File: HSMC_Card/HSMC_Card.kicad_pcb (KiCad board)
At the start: 2 copper layers, 25.4 x 78.1 mm, 5 parts, among them J1 HSMC_Card_ASP

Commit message: Minor adjustments to HSMC_Card PCB
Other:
- board text added: "Host Board Edge 5mm Verical Clearance"
- board text removed: "Host Board Edge 0.5mm Verical Clearance"
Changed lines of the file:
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@@
   (general
     (thickness 1.6)
-    (drawings 5)
+    (drawings 6)
     (tracks 0)
     (zones 0)
@@
     (pad_to_mask_clearance 0.051)
     (solder_mask_min_width 0.25)
-    (aux_axis_origin 0 0)
+    (aux_axis_origin 25.4 25.4)
     (visible_elements FFFFFF7F)
     (pcbplotparams
@@
     (pad "" np_thru_hole circle (at 0 0) (size 3.175 3.175) (drill 3.175) (layers *.Cu *.Mask))
   )
-  (gr_text "Host Board Edge\n0.5mm Verical Clearance" (at 46.99 64.4652 270) (layer Cmts.User)
+  (dimension 78.105 (width 0.3) (layer Cmts.User)
+    (gr_text "3.0760 in" (at 21.395 64.4525 90) (layer Cmts.User)
+      (effects (font (size 1.5 1.5) (thickness 0.3)))
+    )
+    (feature1 (pts (xy 24.765 25.4) (xy 22.908579 25.4)))
+    (feature2 (pts (xy 24.765 103.5304) (xy 22.908579 103.5304)))
+    (crossbar (pts (xy 23.495 103.5304) (xy 23.495 25.4)))
+    (arrow1a (pts (xy 23.495 25.4) (xy 24.081421 26.526504)))
+    (arrow1b (pts (xy 23.495 25.4) (xy 22.908579 26.526504)))
+    (arrow2a (pts (xy 23.495 103.5304) (xy 24.081421 102.378496)))
+    (arrow2b (pts (xy 23.495 103.5304) (xy 22.908579 102.378496)))
+  )
+  (gr_text "Host Board Edge\n5mm Verical Clearance" (at 46.99 64.4652 270) (layer Cmts.User)
     (effects (font (size 1 1) (thickness 0.12)))
   )

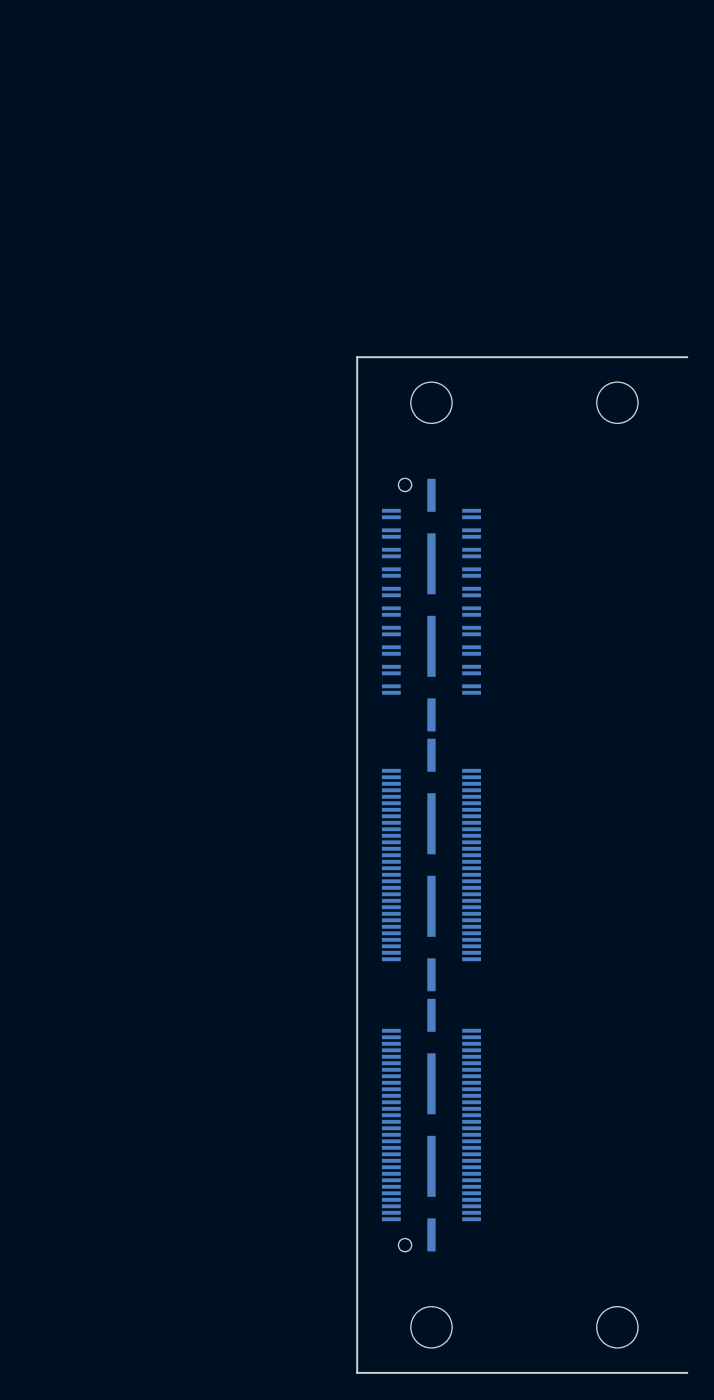
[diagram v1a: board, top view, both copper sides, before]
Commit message: Update version of HSMC_Card_ASP symbol, minor adjustments to PCB layout template.
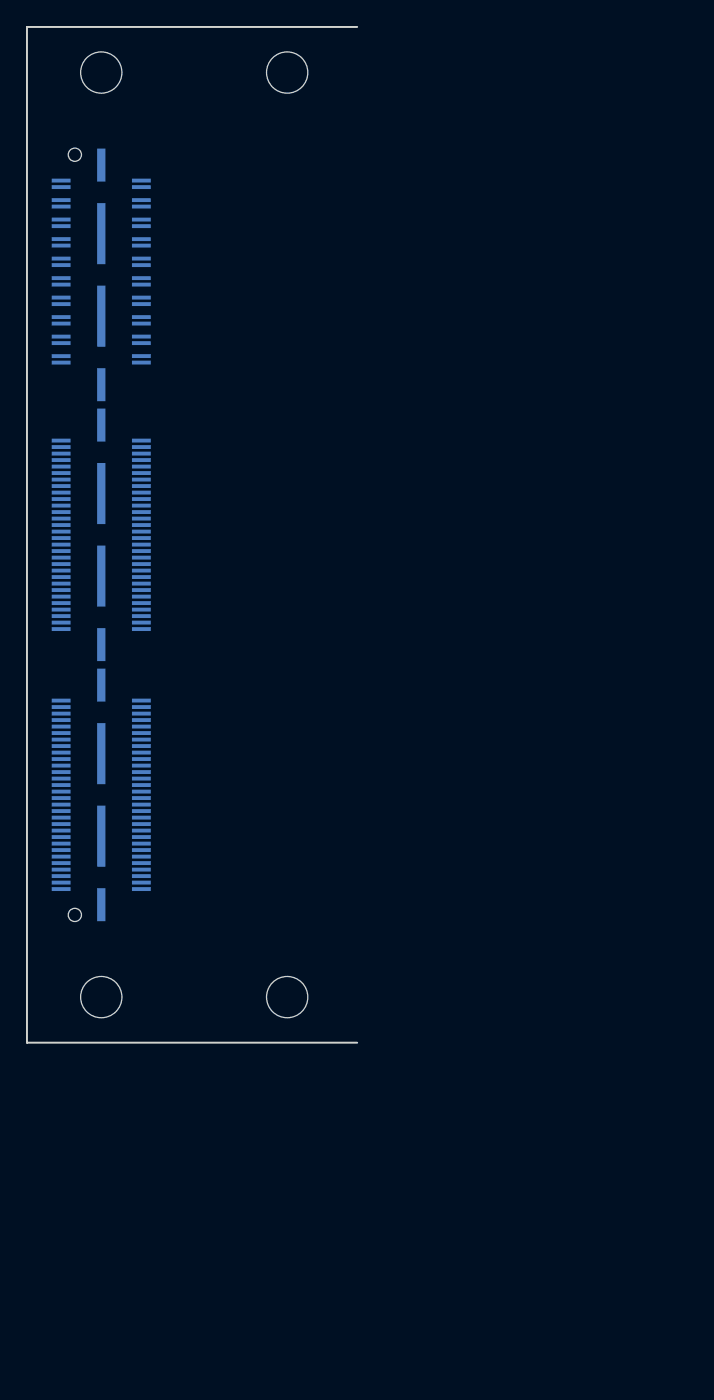
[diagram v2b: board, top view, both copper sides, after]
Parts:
- moved J1 35.9 mm to (5.71, 39.1)
- moved MH1 35.9 mm to (5.71, 3.51)
- moved MH3 35.9 mm to (20.0, 3.51)
- moved MH2 35.9 mm to (5.71, 74.6)
- moved MH4 35.9 mm to (20.0, 74.6)
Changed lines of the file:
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@@
-(kicad_pcb (version 20171130) (host pcbnew 5.0.1)
+(kicad_pcb (version 20171130) (host pcbnew 5.1.1)
   (general
     (thickness 1.6)
@@
     (zone_45_only no)
     (trace_min 0.2)
-    (segment_width 0.2)
-    (edge_width 0.15)
     (via_size 0.8)
     (via_drill 0.4)
@@
     (uvia_min_size 0.2)
     (uvia_min_drill 0.1)
+    (edge_width 0.15)
+    (segment_width 0.2)
     (pcb_text_width 0.3)
     (pcb_text_size 1.5 1.5)
@@
     (pad_to_mask_clearance 0.051)
     (solder_mask_min_width 0.25)
-    (aux_axis_origin 25.4 25.4)
-    (visible_elements FFFFFF7F)
+    (aux_axis_origin 0 0)
+    (visible_elements FEFFFF7F)
     (pcbplotparams
       (layerselection 0x010fc_ffffffff)
@@
     (add_net "Net-(J1-Pad98)")
   )
-  (module Connector_Samtec:Samtec_HSMC_ASP-122952-01_P0.5mm_Vertical locked (layer B.Cu)
-    (at 31.115 64.4652 270)
+  (module Connector_Samtec:Samtec_HSMC_ASP-122952-01_P0.5mm_Vertical (layer B.Cu)
+    (at 5.715 39.0652 270)
     (descr http://suddendocs.samtec.com/prints/asp-122952-01-mkt.pdf)
     (tags "Samtec HSMC card mezzanine vertical")
@@
   )
   (module MountingHole:MoutingHole_0.125in locked (layer F.Cu)
-    (at 45.4152 28.9052)
+    (at 20.0152 3.5052)
     (attr virtual)
     (fp_text reference MH3 (at 0 -4.5) (layer F.SilkS) hide
@@
   )
   (module MountingHole:MoutingHole_0.125in locked (layer F.Cu)
-    (at 45.4152 100.0252)
+    (at 20.0152 74.6252)
     (attr virtual)
     (fp_text reference MH4 (at 0 -4.5) (layer F.SilkS) hide
@@
   )
   (module MountingHole:MoutingHole_0.125in locked (layer F.Cu)
-    (at 31.115 100.0252)
+    (at 5.715 74.6252)
     (attr virtual)
     (fp_text reference MH2 (at 0 -4.5) (layer F.SilkS) hide
@@
   )
   (module MountingHole:MoutingHole_0.125in locked (layer F.Cu)
-    (at 31.115 28.9052)
+    (at 5.715 3.5052)
     (attr virtual)
     (fp_text reference MH1 (at 0 -4.5) (layer F.SilkS) hide
@@
   )
   (dimension 78.105 (width 0.3) (layer Cmts.User)
-    (gr_text "3.0760 in" (at 21.395 64.4525 90) (layer Cmts.User)
+    (gr_text "3.0760 in" (at -4.005 39.0525 90) (layer Cmts.User)
       (effects (font (size 1.5 1.5) (thickness 0.3)))
     )
-    (feature1 (pts (xy 24.765 25.4) (xy 22.908579 25.4)))
-    (feature2 (pts (xy 24.765 103.5304) (xy 22.908579 103.5304)))
-    (crossbar (pts (xy 23.495 103.5304) (xy 23.495 25.4)))
-    (arrow1a (pts (xy 23.495 25.4) (xy 24.081421 26.526504)))
-    (arrow1b (pts (xy 23.495 25.4) (xy 22.908579 26.526504)))
-    (arrow2a (pts (xy 23.495 103.5304) (xy 24.081421 102.378496)))
-    (arrow2b (pts (xy 23.495 103.5304) (xy 22.908579 102.378496)))
-  )
-  (gr_text "Host Board Edge\n5mm Verical Clearance" (at 46.99 64.4652 270) (layer Cmts.User)
+    (feature1 (pts (xy -0.635 0) (xy -2.491421 0)))
+    (feature2 (pts (xy -0.635 78.1304) (xy -2.491421 78.1304)))
+    (crossbar (pts (xy -1.905 78.1304) (xy -1.905 0)))
+    (arrow1a (pts (xy -1.905 0) (xy -1.318579 1.126504)))
+    (arrow1b (pts (xy -1.905 0) (xy -2.491421 1.126504)))
+    (arrow2a (pts (xy -1.905 78.1304) (xy -1.318579 76.978496)))
+    (arrow2b (pts (xy -1.905 78.1304) (xy -2.491421 76.978496)))
+  )
+  (gr_text "Host Board Edge\n5mm Verical Clearance" (at 21.59 39.0652 270) (layer Cmts.User)
     (effects (font (size 1 1) (thickness 0.12)))
   )
-  (gr_line (start 48.8442 25.4) (end 48.8442 103.5304) (layer Cmts.User) (width 0.2))
-  (gr_line (start 25.4 103.5304) (end 50.8 103.5304) (layer Edge.Cuts) (width 0.15))
-  (gr_line (start 25.4 25.4) (end 25.4 103.5304) (layer Edge.Cuts) (width 0.15))
-  (gr_line (start 25.4 25.4) (end 50.8 25.4) (layer Edge.Cuts) (width 0.15))
+  (gr_line (start 23.4442 0) (end 23.4442 78.1304) (layer Cmts.User) (width 0.2))
+  (gr_line (start 0 78.1304) (end 25.4 78.1304) (layer Edge.Cuts) (width 0.15))
+  (gr_line (start 0 0) (end 0 78.1304) (layer Edge.Cuts) (width 0.15))
+  (gr_line (start 0 0) (end 25.4 0) (layer Edge.Cuts) (width 0.15))
 )
